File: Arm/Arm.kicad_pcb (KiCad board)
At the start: 2 copper layers, 91.1 x 109 mm, 61 parts, among them J10 SparkMAX XT60 F, J11 CAN OUT, J12 SparkMAX XT60 F, J13 SparkMAX XT60 F, J14 Encoder 0, J2 Encoder Bundle, J3 CAN IN, J4 5V Swtich Power, J5 Power IN XT60 M, J6 SparkMAX XT60 F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

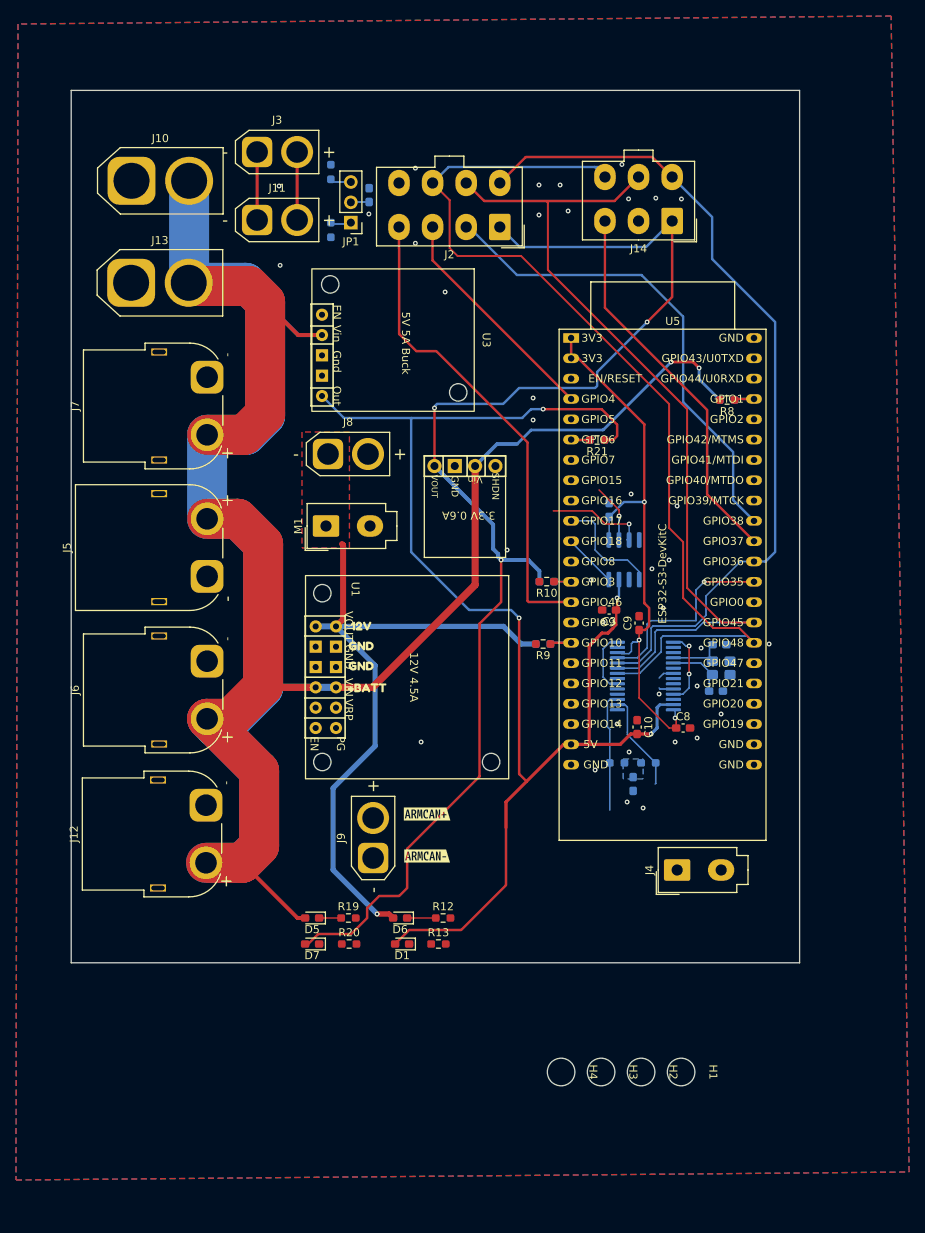
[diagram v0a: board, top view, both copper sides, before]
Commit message: Changes were mostly traces and part spacing
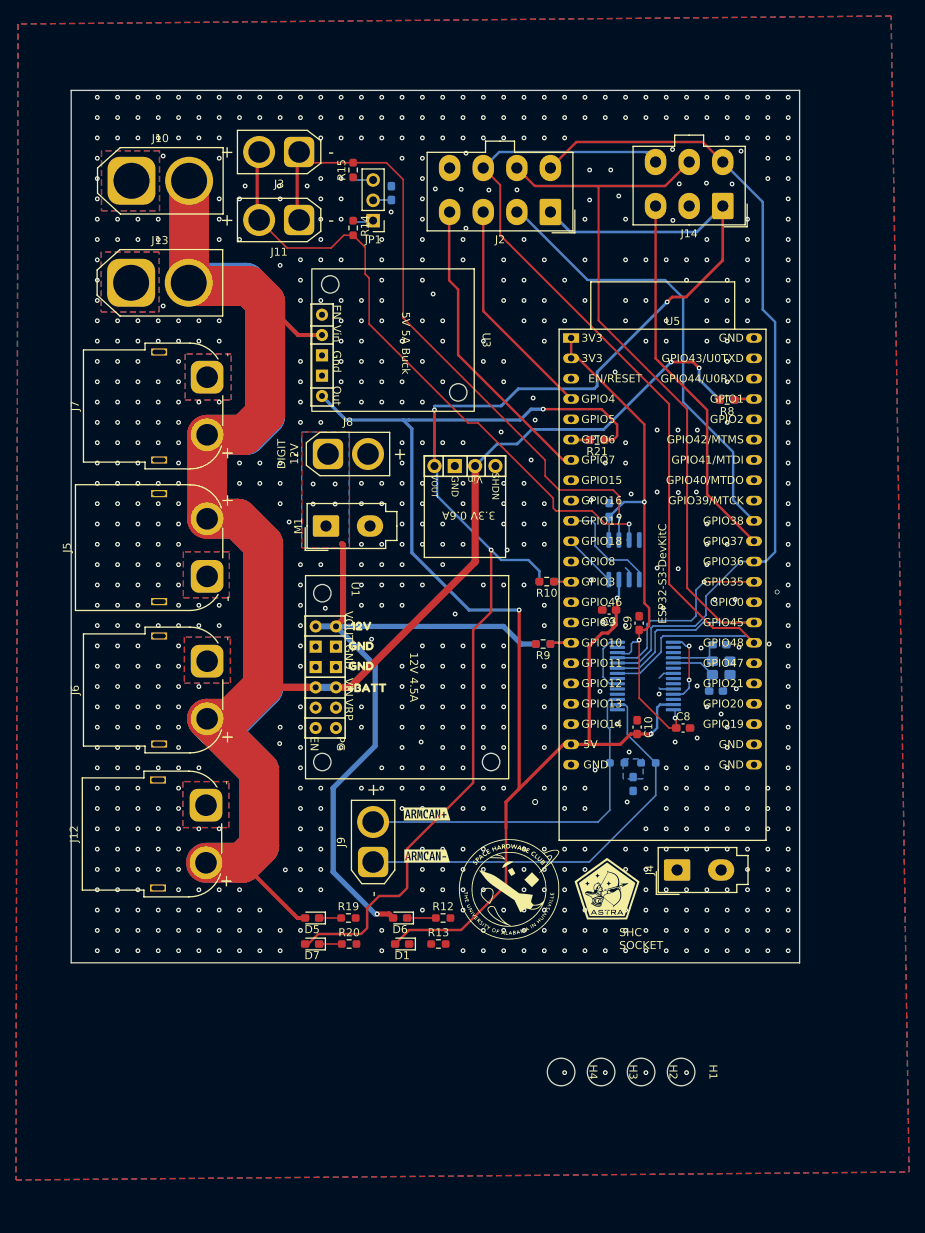
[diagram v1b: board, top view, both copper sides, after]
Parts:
- added G***: LOGO, LOGO, F.Cu at (112.8, 148.5)
- added G***: LOGO, LOGO, F.Cu at (100.8, 148.8)
- R14, R15: moved to F.Cu
- moved J2 6.60 mm to (105.7, 64.0)
- moved J14 6.60 mm to (127.2, 63.2)
- moved J11 5.25 mm to (74.2, 65.0), turned to 180 degrees
- moved J3 5.25 mm to (74.2, 56.5), turned to 180 degrees
- moved C1 2.79 mm to (85.8, 61.6)
- moved JP1 2.79 mm to (83.5, 65.1)
- moved R14 2.79 mm to (81.0, 66.0)
- moved R15 2.79 mm to (81.0, 58.8)
- moved J9 0.50 mm to (83.5, 145.2)
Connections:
- U5 pad 14: /CS_Encoder_3 -> unconnected-(U5-GPIO46-Pad14)
- U5 pad 7: unconnected-(U5-GPIO7/ADC1_CH6-Pad7) -> /CS_Encoder_3
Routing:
- net /Vehicle Control CAN-: track 15.8 -> 83.1 mm
- net /Vehicle Control CAN+: track 21.0 -> 80.2 mm
- net /Arm Motor CAN-: track 11.5 -> 51.7 mm
- net /Arm Motor CAN+: track 16.8 -> 45.2 mm
- net /CS_Encoder_3: track 60.4 -> 37.9 mm
- net +12V: track 83.8 -> 94.7 mm, vias 1 -> 5
- net +3.3V: track 163.0 -> 170.0 mm
- net /CLK_ESP0: track 125.8 -> 120.4 mm
- net /CS_Encoder_1: track 61.0 -> 56.8 mm
- net Net-(D7-K): track 0.00 -> 2.84 mm
- net GND: track 3.86 -> 5.54 mm, vias 37 -> 794
- net +BATT: track 332.4 -> 330.7 mm
- net +5V: track 173.9 -> 175.4 mm
- net /MOSI_ESP0: track 104.6 -> 103.9 mm
- net /CS_Encoder_0: track 47.7 -> 47.0 mm
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- added copper zone on B.Cu, net +12V
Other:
- board text added: "DIGIT 12V"
- board text added: "SHC SOCKET"
- board text added: "SPARKMAX XT#0"

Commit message: No
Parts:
- H1, H2, H3, H4: footprint Arm:4-40 Mounting Hole -> MountingHole:MountingHole_3.2mm_M3
- moved H3 121.5 mm to (134.0, 52.0), turned to 0 degrees
- moved H1 72.9 mm to (51.0, 154.8), turned to 0 degrees
- moved H4 30.4 mm to (132.5, 188.0), turned to 0 degrees
- moved H2 22.3 mm to (131.8, 154.8), turned to 0 degrees
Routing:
- net /ESP0_TX-CAN_TX: track 13.7 -> 12.7 mm
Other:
- board text added: "AXIS0 Encoder"
- board text added: "Arm Encoder"
- board text added: "SPARKMAX XT60"
- board text added: "VICCan"
- board text removed: "SPARKMAX XT#0"

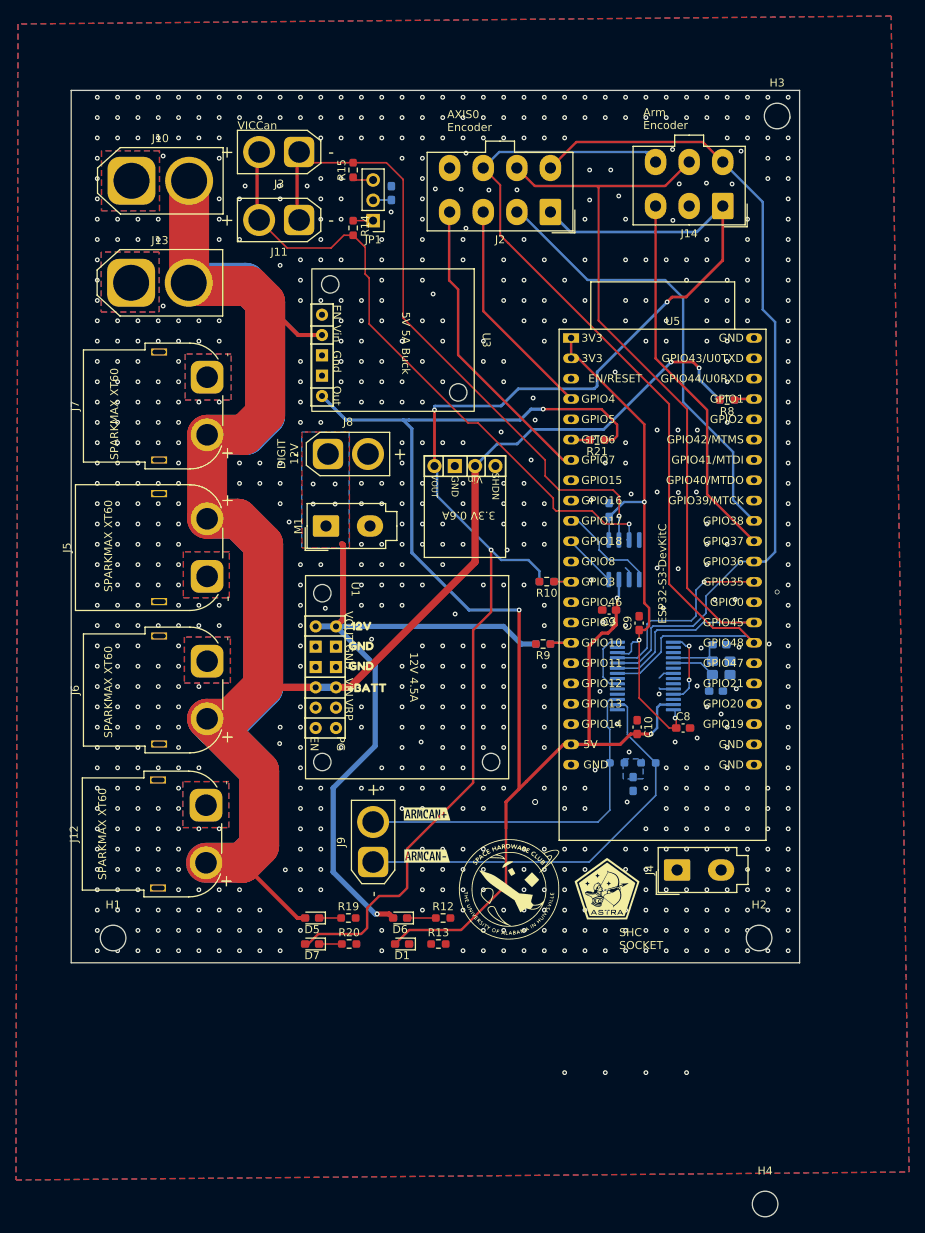
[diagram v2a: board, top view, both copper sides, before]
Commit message: Optimizations
Some Labesl

Mounting Holes

Changed some pins around for short traces
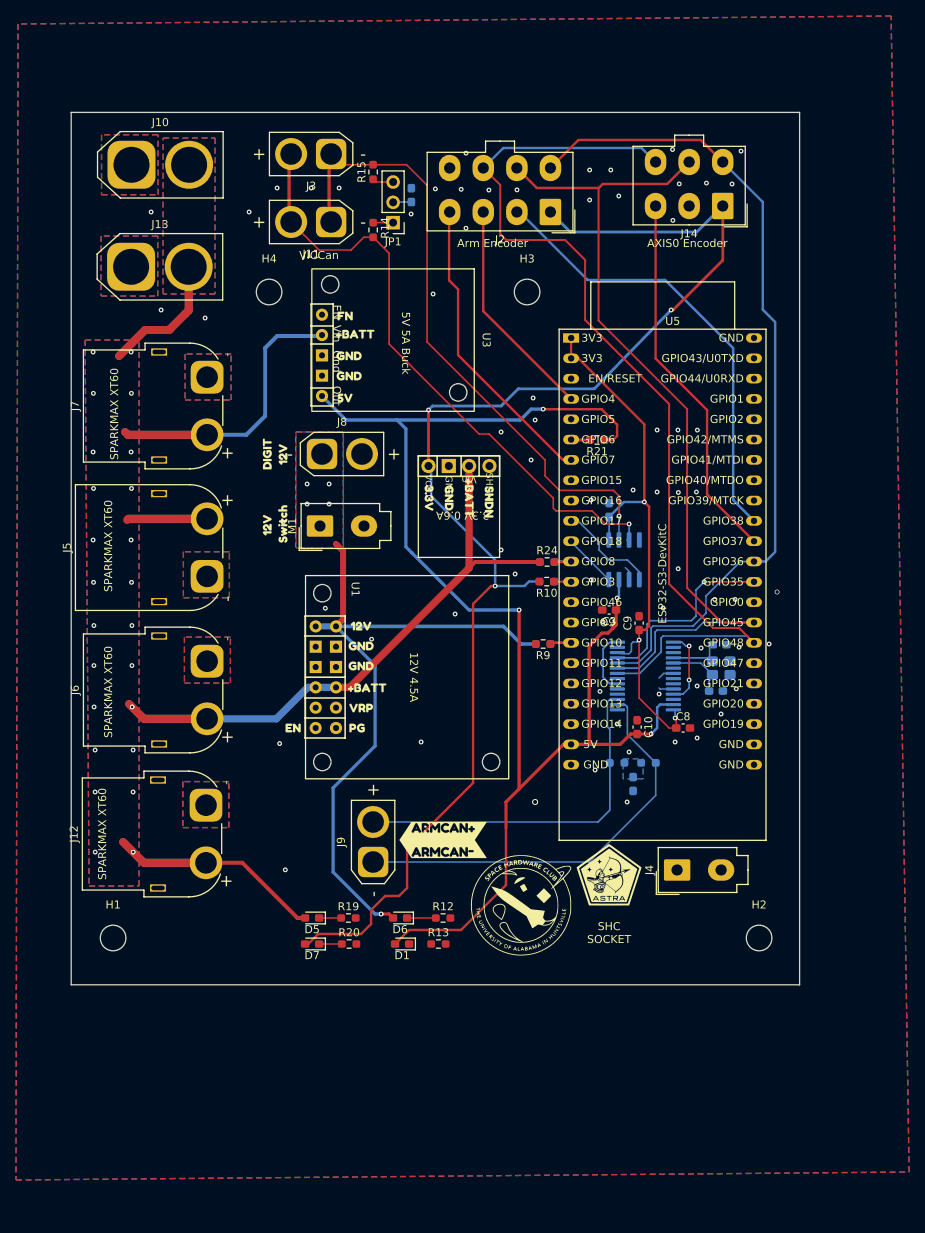
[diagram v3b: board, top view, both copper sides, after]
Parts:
- removed kibuzzard-69541E91: G***, kibuzzard-69541E91
- removed kibuzzard-69541EDE: G***, kibuzzard-69541EDE
- added kibuzzard-696ED45F: G***, kibuzzard-696ED45F, F.Cu at (92.2, 142.5)
- added kibuzzard-696ED4E2: G***, kibuzzard-696ED4E2, F.Cu at (82.0, 126.0)
- added kibuzzard-696ED4F2: G***, kibuzzard-696ED4F2, F.Cu at (73.5, 128.5)
- added kibuzzard-696ED4F9: G***, kibuzzard-696ED4F9, F.Cu at (81.5, 128.5)
- added kibuzzard-696ED84C: G***, kibuzzard-696ED84C, F.Cu at (71.2, 103.0)
- added kibuzzard-696ED85C: G***, kibuzzard-696ED85C, F.Cu at (71.2, 94.2)
- added kibuzzard-696ED8B0: G***, kibuzzard-696ED8B0, F.Cu at (80.0, 87.2)
- added kibuzzard-696EDF62: G***, kibuzzard-696EDF62, F.Cu at (90.5, 99.8)
- added kibuzzard-696EDF69: G***, kibuzzard-696EDF69, F.Cu at (93.0, 99.8)
- added kibuzzard-696EDF70: G***, kibuzzard-696EDF70, F.Cu at (95.5, 99.8)
- added kibuzzard-696EDFA6: G***, kibuzzard-696EDFA6, F.Cu at (98.0, 100.2)
- added kibuzzard-696EDFDB: G***, kibuzzard-696EDFDB, F.Cu at (81.2, 79.3)
- added kibuzzard-696EDFE7: G***, kibuzzard-696EDFE7, F.Cu at (80.5, 82.0)
- added kibuzzard-696EDFF0: G***, kibuzzard-696EDFF0, F.Cu at (80.5, 84.5)
- added kibuzzard-696EE00B: G***, kibuzzard-696EE00B, F.Cu at (80.0, 77.0)
- R24: moved to F.Cu
- R8: moved to B.Cu
- moved H4 129.8 mm to (70.5, 74.0)
- moved H3 38.2 mm to (102.8, 74.0)
- moved R24 30.3 mm to (105.2, 107.8)
- moved R8 30.3 mm to (105.2, 107.8)
- moved J11 4.01 mm to (78.2, 65.2)
- moved J3 4.01 mm to (78.2, 56.8)
- moved C1 2.51 mm to (88.3, 61.9)
- moved JP1 2.51 mm to (86.0, 65.3)
- moved R14 2.51 mm to (83.5, 66.2)
- moved R15 2.51 mm to (83.5, 59.0)
- moved G*** 2.50 mm to (102.2, 150.8)
- moved J10 2.00 mm to (53.3, 58.1)
- moved J13 2.00 mm to (53.2, 70.8)
- moved G*** 1.77 mm to (113.0, 146.8)
- moved J8 0.75 mm to (77.1, 94.2)
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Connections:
- U5 pad 12: unconnected-(U5-GPIO8/ADC1_CH7-Pad12) -> /BATT_ADC
- U5 pad 41: /BATT_ADC -> unconnected-(U5-GPIO1/ADC1_CH0-Pad41)
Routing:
- net +BATT: track 330.7 -> 219.8 mm, vias 2 -> 24
- net /CLK_ESP0: track 120.4 -> 123.3 mm
- net /Vehicle Control CAN+: track 80.2 -> 77.4 mm
- net +3.3V: track 170.0 -> 167.5 mm
- net /Vehicle Control CAN-: track 83.1 -> 81.9 mm
- net /BATT_ADC: track 5.00 -> 4.22 mm
- net +12V: track 94.7 -> 95.3 mm
- net GND: vias 794 -> 68
- added copper zone on B.Cu, net +BATT
- added copper zone on F.Cu, net +BATT
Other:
- board text removed: "DIGIT 12V"

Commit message: Cleaning up things
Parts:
- removed kibuzzard-696ED45F: G***, kibuzzard-696ED45F
- removed kibuzzard-696ED84C: G***, kibuzzard-696ED84C
- removed kibuzzard-696ED85C: G***, kibuzzard-696ED85C
- added G***: LOGO, LOGO, B.Cu at (86.0, 91.0)
- added kibuzzard-696EEF69: G***, kibuzzard-696EEF69, F.Cu at (71.2, 103.0)
- added kibuzzard-696EEF9E: G***, kibuzzard-696EEF9E, F.Cu at (71.2, 94.2)
- added kibuzzard-696EEFE3: G***, kibuzzard-696EEFE3, F.Cu at (69.0, 61.0)
- added kibuzzard-696EF04A: G***, kibuzzard-696EF04A, F.Cu at (89.5, 157.2)
- added kibuzzard-696EF05A: G***, kibuzzard-696EF05A, F.Cu at (78.2, 150.5)
- added kibuzzard-69701E52: G***, kibuzzard-69701E52, F.Cu at (113.2, 155.0)
- added kibuzzard-69702208: G***, kibuzzard-69702208, F.Cu at (78.2, 157.2)
- added kibuzzard-6970222E: G***, kibuzzard-6970222E, F.Cu at (89.5, 150.5)
- added kibuzzard-6970240E: G***, kibuzzard-6970240E, F.Cu at (88.0, 142.5)
- added kibuzzard-69702591: G***, kibuzzard-69702591, F.Cu at (99.0, 68.0)
- added kibuzzard-697025BA: G***, kibuzzard-697025BA, F.Cu at (122.8, 68.0)
- moved G*** 1.27 mm to (102.5, 152.0)
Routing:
- net +3.3V: track 167.5 -> 168.3 mm
- net +BATT: vias 24 -> 29
- added copper zone on F.Cu, net +5V
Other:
- board text removed: "AXIS0 Encoder"
- board text removed: "Arm Encoder"
- board text removed: "SHC SOCKET"
- board text removed: "VICCan"

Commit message: Hegale!
Small optimizations
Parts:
- added G***: LOGO, LOGO, F.Cu at (70.5, 146.4)
- added kibuzzard-69783B26: G***, kibuzzard-69783B26, F.Cu at (120.0, 140.0)
- G***: moved to F.Cu
- moved G*** 61.1 mm to (70.0, 150.0), turned to 45 degrees
- moved J4 13.4 mm to (132.0, 154.5), turned to 180 degrees
- moved H2 8.78 mm to (123.0, 155.5)
- moved G*** 1.12 mm to (103.0, 153.0)
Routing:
- net Net-(D1-K): track 0.00 -> 2.75 mm
- net GND: track 5.54 -> 7.33 mm
- net +3.3V: track 168.3 -> 167.3 mm
- net +BATT: vias 29 -> 24

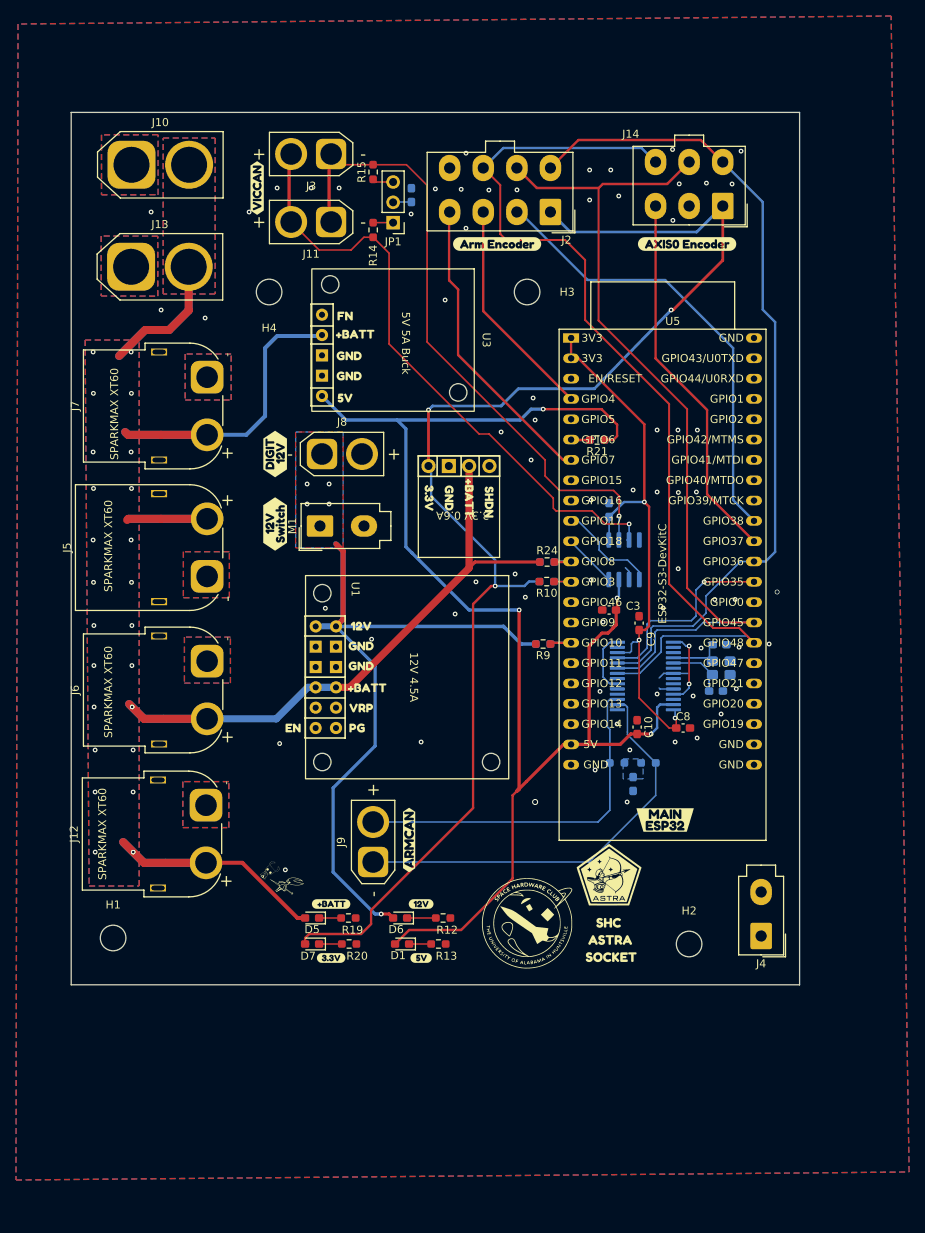
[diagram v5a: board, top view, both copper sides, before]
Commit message: Need to swtich to windows
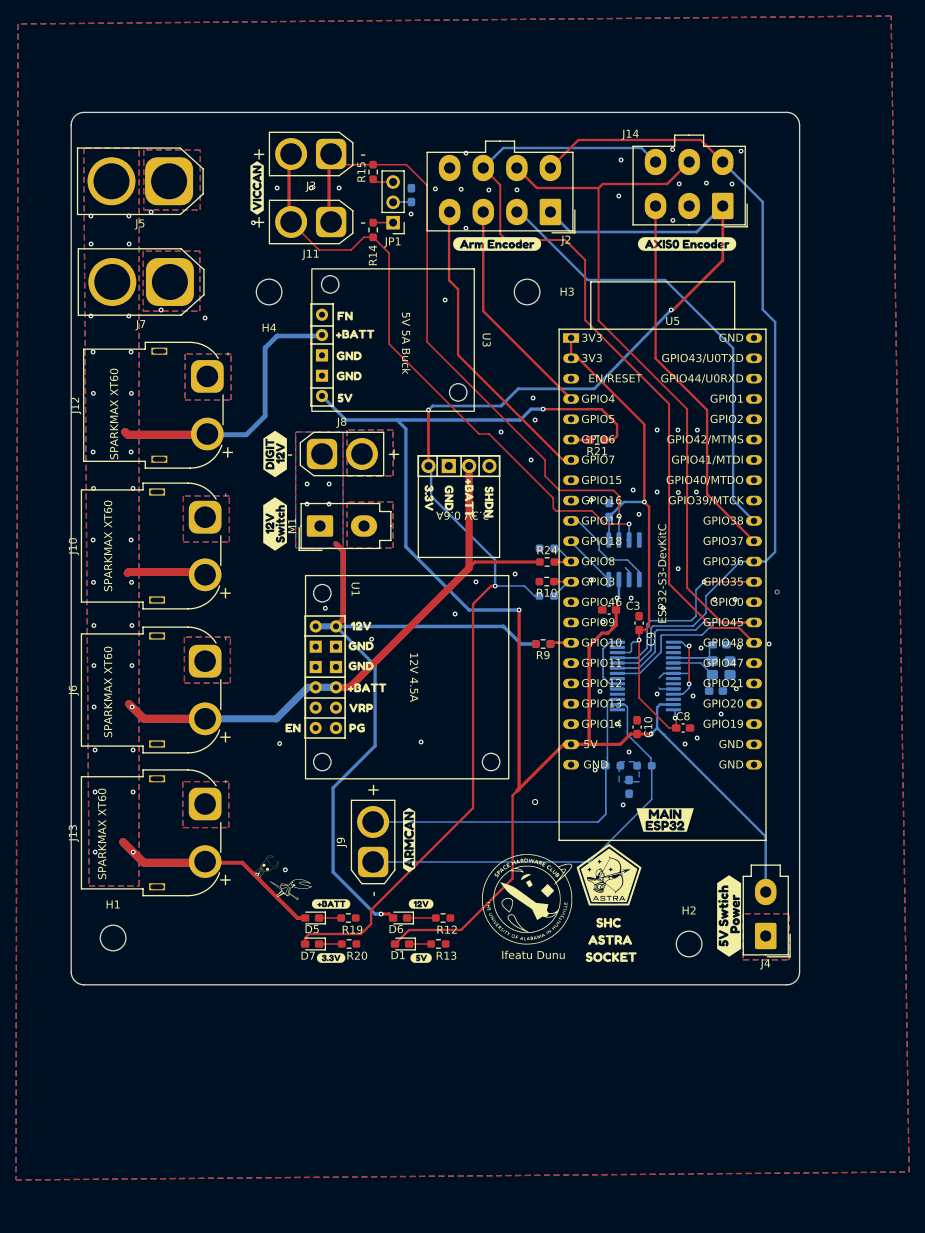
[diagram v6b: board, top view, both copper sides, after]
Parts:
- added kibuzzard-69826405: G***, kibuzzard-69826405, F.Cu at (128.0, 152.0)
- J10: footprint Connector_AMASS:AMASS_XT60-M_1x02_P7.20mm_Vertical -> Connector_AMASS:AMASS_XT60PW-F_1x02_P7.20mm_Horizontal
- J13: footprint Connector_AMASS:AMASS_XT60-F_1x02_P7.20mm_Vertical -> Connector_AMASS:AMASS_XT60PW-F_1x02_P7.20mm_Horizontal
- J5: footprint Connector_AMASS:AMASS_XT60PW-M_1x02_P7.20mm_Horizontal -> Connector_AMASS:AMASS_XT60-M_1x02_P7.20mm_Vertical
- J7: footprint Connector_AMASS:AMASS_XT60PW-F_1x02_P7.20mm_Horizontal -> Connector_AMASS:AMASS_XT60-F_1x02_P7.20mm_Vertical
- moved J13 67.8 mm to (62.5, 138.0), turned to 90 degrees
- moved J12 53.6 mm to (62.8, 84.6)
- moved J5 49.6 mm to (58.0, 60.2), turned to 180 degrees
- moved J10 45.0 mm to (62.5, 102.2), turned to 90 degrees
- moved J7 12.8 mm to (58.1, 72.8), turned to 180 degrees
- moved G*** 3.00 mm to (103.0, 150.0)
- moved R22 1.80 mm to (105.2, 112.0)
- moved R8 1.72 mm to (105.2, 106.0)
- moved G*** 0.66 mm to (70.4, 150.4)
- moved C11 0.62 mm to (115.5, 135.9)
- moved R17 0.62 mm to (117.4, 133.2)
- moved R18 0.62 mm to (113.5, 133.2)
- moved G*** 0.61 mm to (70.1, 145.9)
- moved J4 0.58 mm to (132.6, 154.5)
- moved J6 0.25 mm to (62.5, 120.2)
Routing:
- net +BATT: track 219.8 -> 186.8 mm, vias 24 -> 30
- net +5V: track 175.7 -> 202.1 mm
- net /CLK_ESP0: track 123.3 -> 124.3 mm
- net /3.3V_ADC: track 4.30 -> 5.06 mm
- net /BATT_ADC: track 4.22 -> 4.92 mm
- net GND: vias 68 -> 67
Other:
- outline, holes or cut-outs redrawn
- board text added: "Ifeatu Dunu"
